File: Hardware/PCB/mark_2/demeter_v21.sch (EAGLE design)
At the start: 77 parts, among them IC1 4050, IC2 LM1117-5.0, IC3 LM1117-3.3, IC4 M24C64, IC5 MCP3424, IC6 MCP23017SO, IC7 MAX485, IC8 ATMEGA32U4-AU, Q1 IRLML6402, Q2 IRLML6402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

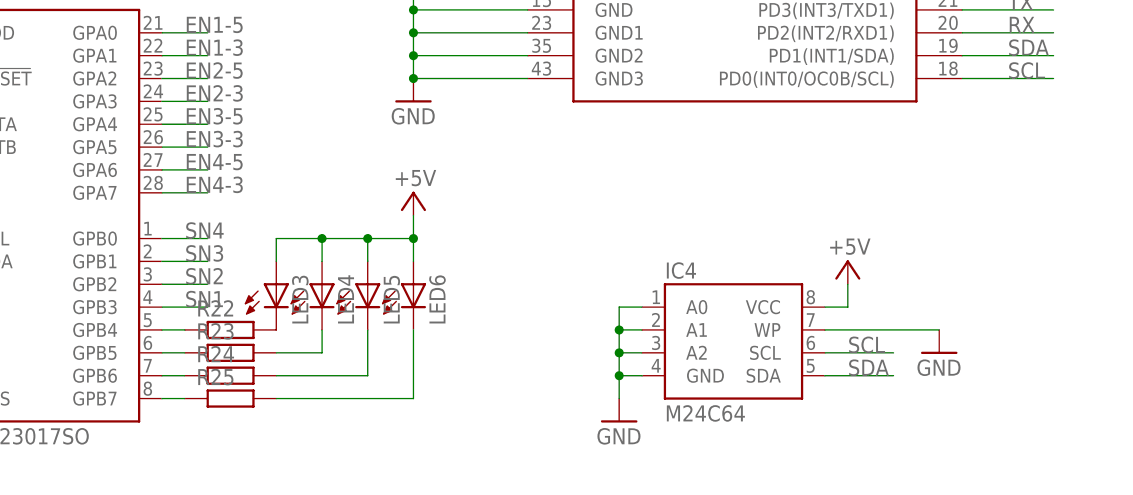
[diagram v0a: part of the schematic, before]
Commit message: 
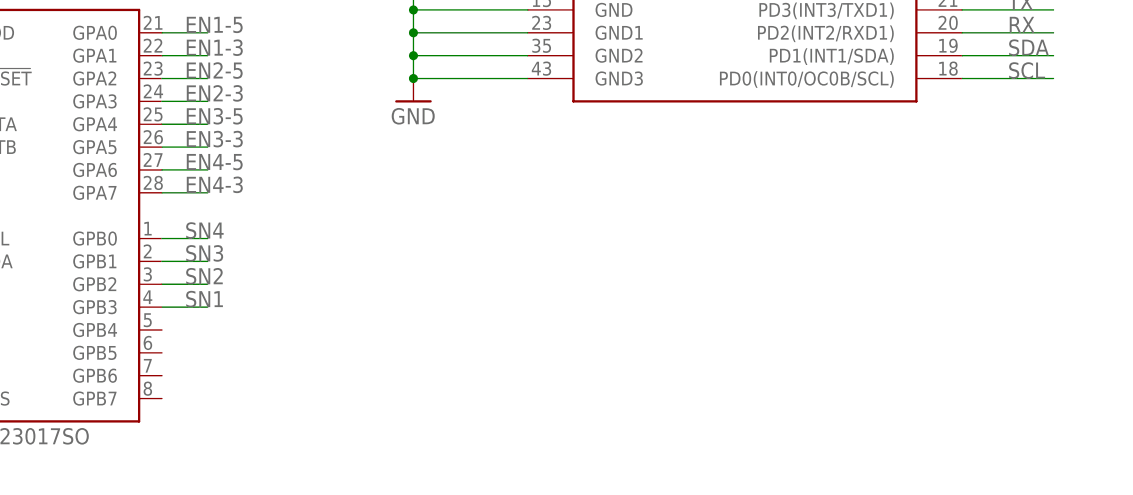
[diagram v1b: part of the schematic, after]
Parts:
- removed IC4: M24C64, mark_2:AT24C
- removed LED3, LED4, LED5, LED6: (no value), mark_2:LED0805
- removed R22, R23, R24, R25: (no value), mark_2:R-EU_R0805
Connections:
- removed net N$37: LED3.C, R22.2
- removed net N$39: LED4.C, R23.2
- removed net N$40: LED5.C, R24.2
- removed net N$41: LED6.C, R25.2
- removed net N$42: IC6.GPB7, R25.1
- removed net N$43: IC6.GPB6, R24.1
- removed net N$44: IC6.GPB5, R23.1
- removed net N$45: IC6.GPB4, R22.1
- net +5V: no longer IC4.VCC, LED3.A, LED4.A, LED5.A, LED6.A
- net GND: no longer IC4.A0, IC4.A1, IC4.A2, IC4.GND, IC4.WP
- net SCL: no longer IC4.SCL
- net SDA: no longer IC4.SDA
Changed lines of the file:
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@@
 <part name="IC7" library="mark_2" deviceset="MAX485" device=""/>
 <part name="X1" library="mark_2" deviceset="W237-103" device=""/>
-<part name="IC4" library="mark_2" deviceset="AT24C*" device="" value="M24C64"/>
-<part name="P+7" library="mark_2" deviceset="+5V" device=""/>
-<part name="GND10" library="mark_2" deviceset="GND" device=""/>
-<part name="GND12" library="mark_2" deviceset="GND" device=""/>
 <part name="Q1" library="mark_2" deviceset="IRLML6402" device=""/>
 <part name="GND13" library="mark_2" deviceset="GND" device=""/>
@@
 <part name="GND28" library="mark_2" deviceset="GND" device=""/>
 <part name="JP2" library="mark_2" deviceset="JUMPER-2" device="SMD-NO"/>
-<part name="R22" library="mark_2" deviceset="R-EU_" device="R0805"/>
-<part name="R23" library="mark_2" deviceset="R-EU_" device="R0805"/>
-<part name="R24" library="mark_2" deviceset="R-EU_" device="R0805"/>
-<part name="R25" library="mark_2" deviceset="R-EU_" device="R0805"/>
-<part name="LED3" library="mark_2" deviceset="LED" device="0805"/>
-<part name="LED4" library="mark_2" deviceset="LED" device="0805"/>
-<part name="LED5" library="mark_2" deviceset="LED" device="0805"/>
-<part name="LED6" library="mark_2" deviceset="LED" device="0805"/>
-<part name="P+19" library="mark_2" deviceset="+5V" device=""/>
 <part name="JP3" library="mark_2" deviceset="JUMPER-3" device="SMD"/>
 <part name="JP4" library="mark_2" deviceset="JUMPER-3" device="SMD"/>
@@
 <instance part="IC7" gate="G$1" x="251.46" y="203.2"/>
 <instance part="X1" gate="G$1" x="276.86" y="200.66"/>
-<instance part="IC4" gate="G$1" x="121.92" y="-5.08"/>
-<instance part="P+7" gate="1" x="134.62" y="2.54" smashed="yes">
-<attribute name="VALUE" x="137.16" y="5.08" size="1.778" layer="96" rot="R180"/>
-</instance>
-<instance part="GND10" gate="1" x="109.22" y="-15.24"/>
-<instance part="GND12" gate="1" x="144.78" y="-7.62"/>
 <instance part="Q1" gate="G$1" x="-10.16" y="139.7" smashed="yes">
 <attribute name="NAME" x="-3.81" y="137.16" size="1.778" layer="95" rot="R180"/>
@@
 <instance part="GND28" gate="1" x="154.94" y="73.66"/>
 <instance part="JP2" gate="A" x="160.02" y="78.74" rot="R270"/>
-<instance part="R22" gate="G$1" x="66.04" y="-5.08"/>
-<instance part="R23" gate="G$1" x="66.04" y="-7.62"/>
-<instance part="R24" gate="G$1" x="66.04" y="-10.16"/>
-<instance part="R25" gate="G$1" x="66.04" y="-12.7"/>
-<instance part="LED3" gate="G$1" x="71.12" y="0"/>
-<instance part="LED4" gate="G$1" x="76.2" y="0"/>
-<instance part="LED5" gate="G$1" x="81.28" y="0"/>
-<instance part="LED6" gate="G$1" x="86.36" y="0"/>
-<instance part="P+19" gate="1" x="86.36" y="10.16" smashed="yes">
-<attribute name="VALUE" x="88.9" y="12.7" size="1.778" layer="96" rot="R180"/>
-</instance>
 <instance part="JP3" gate="G$1" x="200.66" y="203.2" rot="R270"/>
 <instance part="JP4" gate="G$1" x="200.66" y="187.96" rot="R270"/>
@@
 <pinref part="X1" gate="G$1" pin="3"/>
 <wire x1="274.32" y1="198.12" x2="266.7" y2="198.12" width="0.1524" layer="91"/>
-</segment>
-<segment>
-<pinref part="IC4" gate="G$1" pin="WP"/>
-<pinref part="GND12" gate="1" pin="GND"/>
-<wire x1="132.08" y1="-5.08" x2="144.78" y2="-5.08" width="0.1524" layer="91"/>
 </segment>
 <segment>
@@
 <pinref part="GND21" gate="1" pin="GND"/>
 <wire x1="-22.86" y1="-7.62" x2="-25.4" y2="-7.62" width="0.1524" layer="91"/>
-</segment>
-<segment>
-<pinref part="GND10" gate="1" pin="GND"/>
-<wire x1="109.22" y1="-12.7" x2="109.22" y2="-10.16" width="0.1524" layer="91"/>
-<pinref part="IC4" gate="G$1" pin="A0"/>
-<wire x1="109.22" y1="-10.16" x2="109.22" y2="-7.62" width="0.1524" layer="91"/>
-<wire x1="109.22" y1="-7.62" x2="109.22" y2="-5.08" width="0.1524" layer="91"/>
-<wire x1="109.22" y1="-5.08" x2="109.22" y2="-2.54" width="0.1524" layer="91"/>
-<wire x1="109.22" y1="-2.54" x2="111.76" y2="-2.54" width="0.1524" layer="91"/>
-<junction x="109.22" y="-5.08"/>
-<junction x="109.22" y="-7.62"/>
-<junction x="109.22" y="-10.16"/>
-<pinref part="IC4" gate="G$1" pin="GND"/>
-<wire x1="111.76" y1="-10.16" x2="109.22" y2="-10.16" width="0.1524" layer="91"/>
-<pinref part="IC4" gate="G$1" pin="A2"/>
-<wire x1="111.76" y1="-7.62" x2="109.22" y2="-7.62" width="0.1524" layer="91"/>
-<pinref part="IC4" gate="G$1" pin="A1"/>
-<wire x1="111.76" y1="-5.08" x2="109.22" y2="-5.08" width="0.1524" layer="91"/>
 </segment>
 <segment>
@@
 </segment>
 <segment>
-<pinref part="IC4" gate="G$1" pin="VCC"/>
-<pinref part="P+7" gate="1" pin="+5V"/>
-<wire x1="132.08" y1="-2.54" x2="134.62" y2="-2.54" width="0.1524" layer="91"/>
-<wire x1="134.62" y1="-2.54" x2="134.62" y2="0" width="0.1524" layer="91"/>
-</segment>
-<segment>
 <pinref part="IC5" gate="A" pin="VCC"/>
 <pinref part="P+10" gate="1" pin="+5V"/>
@@
 <pinref part="P+18" gate="1" pin="+5V"/>
 </segment>
-<segment>
-<pinref part="LED3" gate="G$1" pin="A"/>
-<wire x1="71.12" y1="2.54" x2="71.12" y2="5.08" width="0.1524" layer="91"/>
-<pinref part="LED6" gate="G$1" pin="A"/>
-<wire x1="71.12" y1="5.08" x2="76.2" y2="5.08" width="0.1524" layer="91"/>
-<wire x1="76.2" y1="5.08" x2="81.28" y2="5.08" width="0.1524" layer="91"/>
-<wire x1="81.28" y1="5.08" x2="86.36" y2="5.08" width="0.1524" layer="91"/>
-<wire x1="86.36" y1="5.08" x2="86.36" y2="2.54" width="0.1524" layer="91"/>
-<junction x="76.2" y="5.08"/>
-<junction x="81.28" y="5.08"/>
-<pinref part="LED4" gate="G$1" pin="A"/>
-<wire x1="76.2" y1="2.54" x2="76.2" y2="5.08" width="0.1524" layer="91"/>
-<pinref part="LED5" gate="G$1" pin="A"/>
-<wire x1="81.28" y1="2.54" x2="81.28" y2="5.08" width="0.1524" layer="91"/>
-<junction x="86.36" y="5.08"/>
-<pinref part="P+19" gate="1" pin="+5V"/>
-<wire x1="86.36" y1="7.62" x2="86.36" y2="5.08" width="0.1524" layer="91"/>
-</segment>
 </net>
 <net name="EN" class="0">
@@
 <net name="SCL" class="0">
 <segment>
-<pinref part="IC4" gate="G$1" pin="SCL"/>
-<wire x1="132.08" y1="-7.62" x2="139.7" y2="-7.62" width="0.1524" layer="91"/>
-<label x="134.62" y="-7.62" size="1.778" layer="95"/>
-</segment>
-<segment>
 <pinref part="IC5" gate="A" pin="SCL"/>
 <wire x1="30.48" y1="63.5" x2="22.86" y2="63.5" width="0.1524" layer="91"/>
@@
 </net>
 <net name="SDA" class="0">
-<segment>
-<pinref part="IC4" gate="G$1" pin="SDA"/>
-<wire x1="132.08" y1="-10.16" x2="139.7" y2="-10.16" width="0.1524" layer="91"/>
-<label x="134.62" y="-10.16" size="1.778" layer="95"/>
-</segment>
 <segment>
 <pinref part="IC5" gate="A" pin="SDA"/>
@@
 </segment>
 </net>
-<net name="N$37" class="0">
-<segment>
-<pinref part="R22" gate="G$1" pin="2"/>
-<pinref part="LED3" gate="G$1" pin="C"/>
-</segment>
-</net>
-<net name="N$39" class="0">
-<segment>
-<pinref part="R23" gate="G$1" pin="2"/>
-<pinref part="LED4" gate="G$1" pin="C"/>
-<wire x1="71.12" y1="-7.62" x2="76.2" y2="-7.62" width="0.1524" layer="91"/>
-<wire x1="76.2" y1="-7.62" x2="76.2" y2="-5.08" width="0.1524" layer="91"/>
-</segment>
-</net>
-<net name="N$40" class="0">
-<segment>
-<pinref part="R24" gate="G$1" pin="2"/>
-<pinref part="LED5" gate="G$1" pin="C"/>
-<wire x1="71.12" y1="-10.16" x2="81.28" y2="-10.16" width="0.1524" layer="91"/>
-<wire x1="81.28" y1="-10.16" x2="81.28" y2="-5.08" width="0.1524" layer="91"/>
-</segment>
-</net>
-<net name="N$41" class="0">
-<segment>
-<pinref part="R25" gate="G$1" pin="2"/>
-<pinref part="LED6" gate="G$1" pin="C"/>
-<wire x1="71.12" y1="-12.7" x2="86.36" y2="-12.7" width="0.1524" layer="91"/>
-<wire x1="86.36" y1="-12.7" x2="86.36" y2="-5.08" width="0.1524" layer="91"/>
-</segment>
-</net>
-<net name="N$42" class="0">
-<segment>
-<pinref part="R25" gate="G$1" pin="1"/>
-<pinref part="IC6" gate="G$1" pin="GPB7"/>
-<wire x1="60.96" y1="-12.7" x2="58.42" y2="-12.7" width="0.1524" layer="91"/>
-</segment>
-</net>
-<net name="N$43" class="0">
-<segment>
-<pinref part="R24" gate="G$1" pin="1"/>
-<pinref part="IC6" gate="G$1" pin="GPB6"/>
-<wire x1="60.96" y1="-10.16" x2="58.42" y2="-10.16" width="0.1524" layer="91"/>
-</segment>
-</net>
-<net name="N$44" class="0">
-<segment>
-<pinref part="R23" gate="G$1" pin="1"/>
-<pinref part="IC6" gate="G$1" pin="GPB5"/>
-<wire x1="60.96" y1="-7.62" x2="58.42" y2="-7.62" width="0.1524" layer="91"/>
-</segment>
-</net>
-<net name="N$45" class="0">
-<segment>
-<pinref part="R22" gate="G$1" pin="1"/>
-<pinref part="IC6" gate="G$1" pin="GPB4"/>
-<wire x1="60.96" y1="-5.08" x2="58.42" y2="-5.08" width="0.1524" layer="91"/>
-</segment>
-</net>
